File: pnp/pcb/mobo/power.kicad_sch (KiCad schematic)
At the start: 28 parts, among them J12 Power, U11 FDS4435BZ, U12 TPS54331, U13 AP1117-33

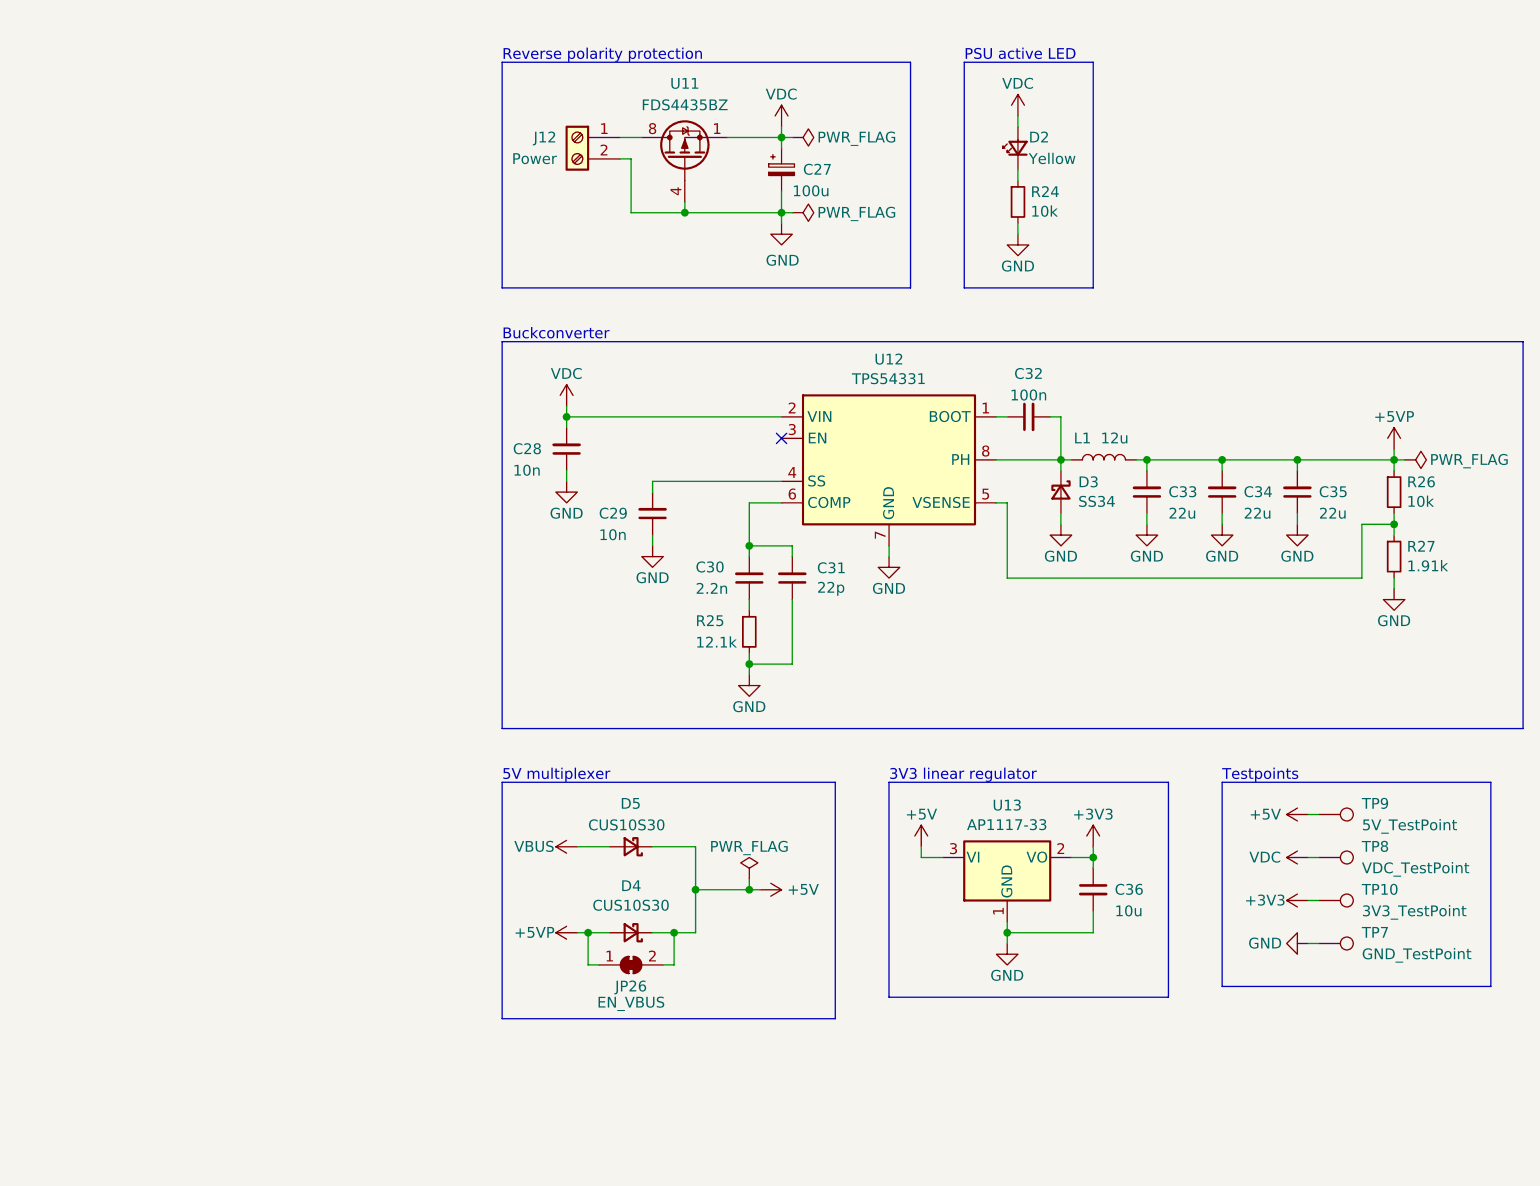
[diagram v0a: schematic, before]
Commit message: first commit of rev04 mobo beta 0. makes solder-selectable jumpers on back side of board not jumped to work with kit drivers, y2 motor port rotated correctly, moves traces out from underneath solder jumpers, adds 0 ohm jumpers to bypass the usb hub, adds 4 pin DIN connector for power, adds large decoupling cap on power supply input to decrease rippling, changes diode choice for 5v multiplexer to one already in the BOM, flips resistors on mos1 to be less confusing
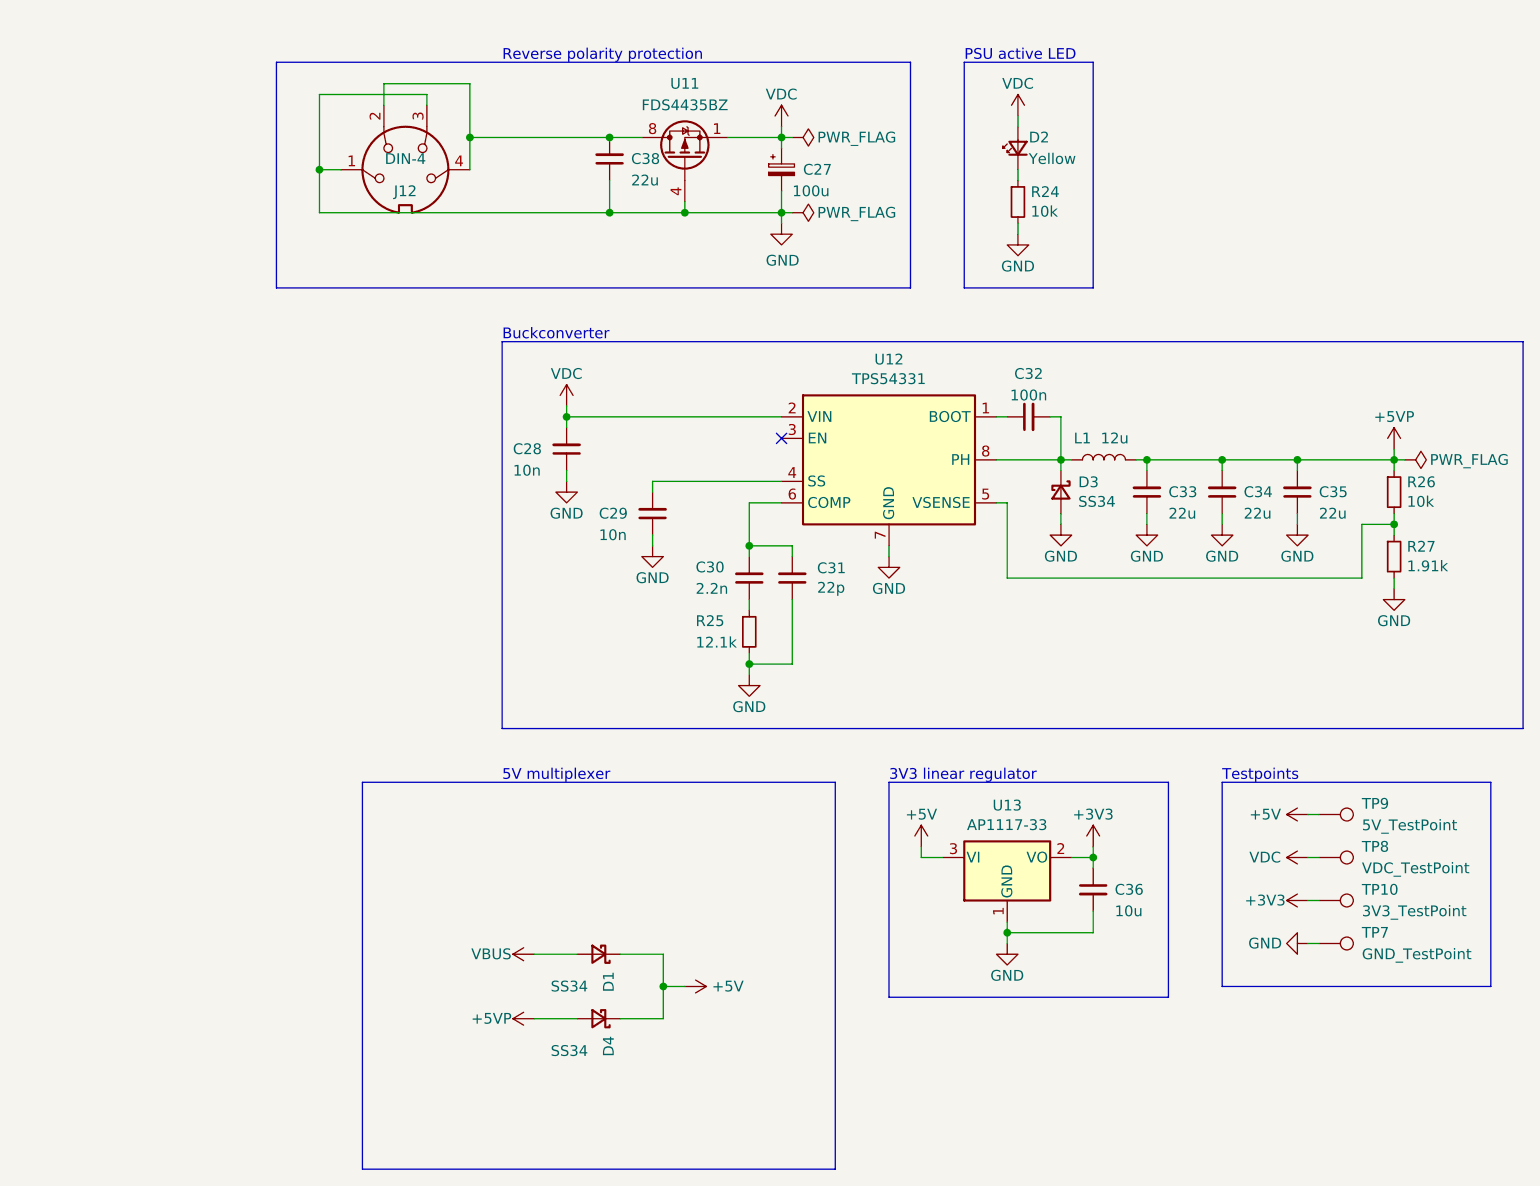
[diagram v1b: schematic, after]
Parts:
- removed D5: CUS10S30, Diode_SMD:D_SOD-323, symbol Device:D_Schottky_Small
- removed J12: Power, TerminalBlock_Phoenix:TerminalBlock_Phoenix_MKDS-1,5-2_1x02_P5.00mm_Horizontal, symbol Connector:Screw_Terminal_01x02
- removed JP26: EN_VBUS, Jumper:SolderJumper-2_P1.3mm_Bridged_RoundedPad1.0x1.5mm, symbol Jumper:SolderJumper_2_Bridged
- added C38: 22u, Capacitor_SMD:C_0805_2012Metric, symbol Device:C_Small
- added D1: SS34, Diode_SMD:D_SMA, symbol Device:D_Schottky_Small
- added J12: DIN-4, index:KPJX-4S-S, symbol Connector:DIN-4
- D4: value CUS10S30 -> SS34; footprint Diode_SMD:D_SOD-323 -> Diode_SMD:D_SMA; Config +USBPWR -> (none); Digikey (none) -> 641-2115-1-ND; JLCPCB C146335 -> C8678; LCSC C146335 -> C266553; Mouser (none) -> 821-SS34LRVG; Notes (none) -> Vf<=0.55V,I>=2A,Vr>=24V
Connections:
- net +5V: now also D1.1 (K)
- net GND: now also C38.1, J12.1, J12.3
- net VBUS: now also D1.2 (A)
- net at U11.5 (D), U11.6 (D), U11.7 (D)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: now also C38.2, J12.2, J12.4

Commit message: another huge chunk of work on rev04 of the mobo. breaks out diag and index pin for TMC2209 sensorless homing. reduces unique part count by consolidating resistor values where possible. replaces full ADC pipeline with monolithic I2C vacuum sensor and an I2C multiplexer due to address collision issues with two sensors. adds solder selectable jumpers for selecting whether an axis uses switch or TMC homing. redoes lots of routing of the SPI lines up to the stepper drivers.
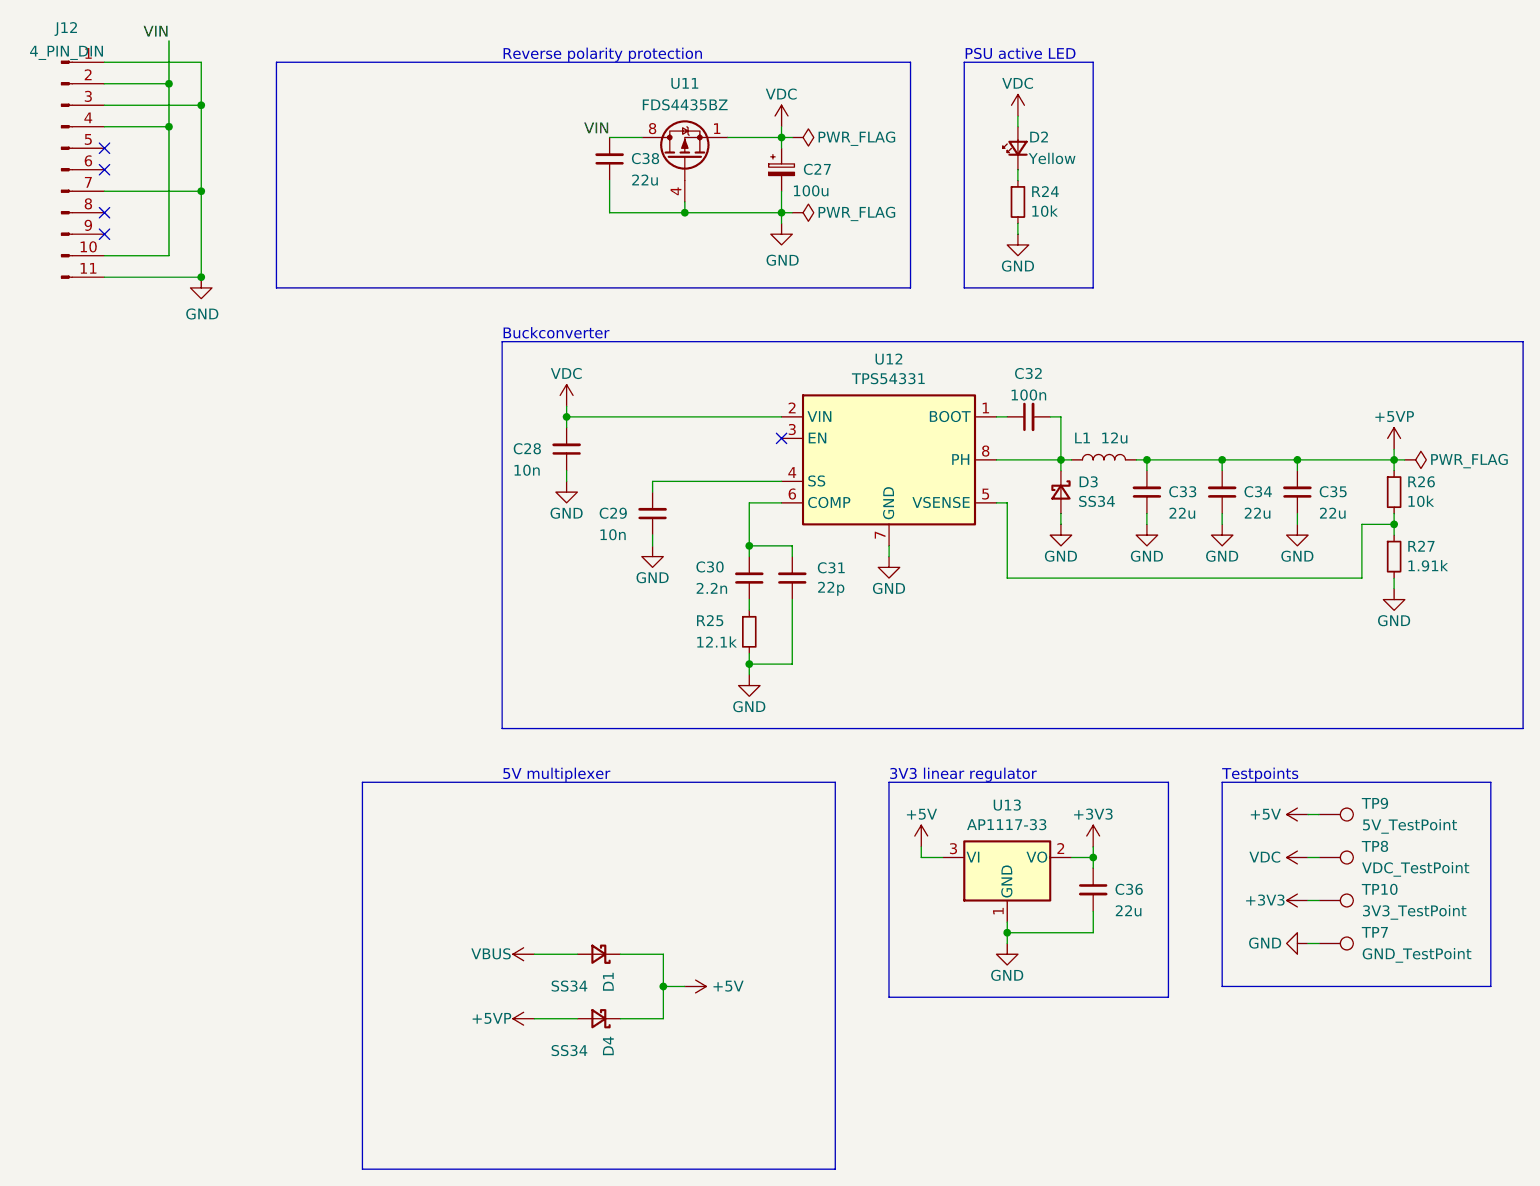
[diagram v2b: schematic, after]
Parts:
- removed J12: DIN-4, index:KPJX-4S-S, symbol Connector:DIN-4
- added J12: 4_PIN_DIN, index:KPJX-4S-S, symbol Connector:Conn_01x11_Male
- C36: value 10u -> 22u
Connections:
- net GND: now also J12.1 (Pin_1), J12.11 (Pin_11), J12.3 (Pin_3), J12.7 (Pin_7)
- net VIN: now reaches C38.2, U11.5 (D), U11.6 (D), U11.7 (D), U11.8 (D)
- net VIN: now also J12.10 (Pin_10), J12.2 (Pin_2), J12.4 (Pin_4)
- no-connect marks 1 -> 5
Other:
- company: (none) -> Opulo
- title: Power -> LumenPnP Motherboard

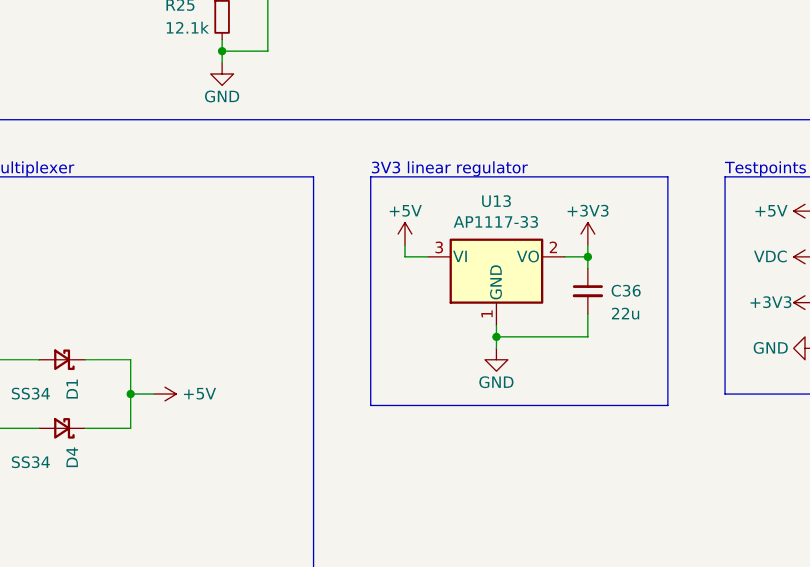
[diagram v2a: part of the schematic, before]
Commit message: fixes erc errors about pin connectivity
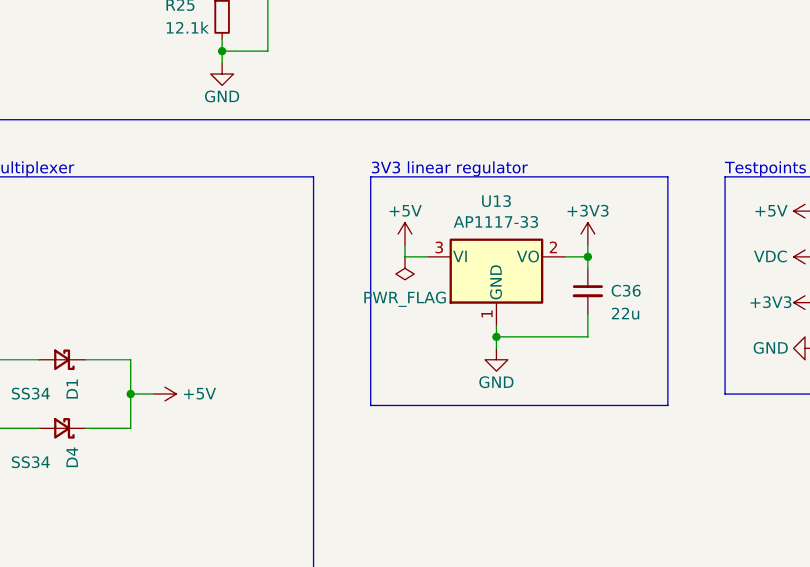
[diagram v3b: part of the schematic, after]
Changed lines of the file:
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@@
+    (pin "1")
+  )
+  (symbol (lib_id "power:PWR_FLAG") (at 138.43 140.97 180) (unit 1)
+    (in_bom yes) (on_board yes) (fields_autoplaced)
+    (property "Reference" "#FLG0105" (id 0) (at 138.43 142.875 0)
+      (effects (font (size 1.27 1.27)) hide)
+    )
+    (property "Value" "PWR_FLAG" (id 1) (at 138.43 145.5325 0))
+    (property "Footprint" "" (id 2) (at 138.43 140.97 0)
+      (effects (font (size 1.27 1.27)) hide)
+    )
+    (property "Datasheet" "~" (id 3) (at 138.43 140.97 0)
+      (effects (font (size 1.27 1.27)) hide)
+    )
     (pin "1")
   )
